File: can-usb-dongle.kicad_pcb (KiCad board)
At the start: 2 copper layers, 30 x 15 mm, 42 parts, among them SW1 SW_PUSH, U1 STM32F302C8T, U2 SN65HVD256, U3 NUF2042XV6, U4 MCP1700, U5 SiP32431, X1 16MHz 10ppm

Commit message: optimize traces
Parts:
- C12: moved to B.Cu
- moved C13 6.56 mm to (48.0, 38.5), turned to 180 degrees
- moved C11 4.26 mm to (54.5, 39.0), turned to 90 degrees
- moved R10 2.83 mm to (65.8, 40.8), turned to 270 degrees
- moved C6 2.75 mm to (57.8, 45.0)
- moved C5 2.70 mm to (59.0, 46.8)
- moved R2 2.66 mm to (49.0, 40.2)
- moved C9 2.55 mm to (59.5, 42.2), turned to 270 degrees
- moved C12 2.51 mm to (52.5, 39.5)
- moved C15 2.50 mm to (56.2, 43.0), turned to 90 degrees
- moved F1 2.26 mm to (51.0, 38.5), turned to 180 degrees
- moved R11 2.24 mm to (67.2, 40.8), turned to 270 degrees
- moved R5 1.82 mm to (49.2, 51.5), turned to 180 degrees
- moved R8 1.35 mm to (52.5, 48.8), turned to 90 degrees
- moved U4 1.25 mm to (52.8, 40.5)
- moved R4 1.12 mm to (64.5, 39.2), turned to 90 degrees
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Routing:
- net GND: track 52.0 -> 146.0 mm, vias 1 -> 7
- net VCC: track 38.8 -> 71.1 mm, vias 4 -> 5
- net /V_BUS_SENSE: track 19.6 -> 11.8 mm
- net /USB_D-: track 4.62 -> 11.9 mm
- net /USB_D+: track 10.3 -> 17.2 mm
- net /UART1_RX: track 11.8 -> 7.02 mm
- net /V_USB: track 26.7 -> 22.9 mm
- net /UART1_TX: track 10.8 -> 8.17 mm
- net /STATUS_LED: track 8.98 -> 6.57 mm
- net /NRST: track 9.60 -> 11.8 mm
- net Net-(C13-Pad1): track 10.4 -> 12.3 mm
- net Net-(CONN1-Pad4): track 10.3 -> 8.54 mm
- net /V_CAN_BUS: track 22.1 -> 23.7 mm
- net /CAN1_TX: track 5.64 -> 4.27 mm
- net Net-(D1-Pad2): track 0.00 -> 1.35 mm
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
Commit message: Better LED placement, change VCC routing
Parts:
- C10: moved to B.Cu
- moved R9 4.72 mm to (66.8, 47.0), turned to 90 degrees
- moved R3 3.26 mm to (63.5, 40.5)
- moved R4 3.26 mm to (61.2, 39.5)
- moved C10 2.26 mm to (67.8, 48.8), turned to 0 degrees
- moved R7 1.41 mm to (65.2, 50.2), turned to 0 degrees
- moved C14 1.00 mm to (68.2, 47.0)
- moved D2 0.35 mm to (67.8, 51.5)
- moved D3 0.35 mm to (67.8, 50.2)
- moved R6 0.35 mm to (65.2, 51.5), turned to 0 degrees
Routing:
- net GND: track 146.0 -> 170.7 mm
- net VCC: track 71.1 -> 64.9 mm
- net Net-(D3-Pad2): track 3.97 -> 0.00 mm
- net /V_BUS_SENSE: track 11.8 -> 8.48 mm
- net /V_CAN_BUS: track 23.7 -> 26.7 mm
- net /USB_D+: track 17.2 -> 19.1 mm
- net Net-(D2-Pad2): track 1.88 -> 0.00 mm
- net Net-(C7-Pad2): track 2.94 -> 4.76 mm
- net /CAN1_PWR_LED: track 7.46 -> 5.76 mm
- net /USB_D-: track 11.9 -> 13.2 mm
- net /CAN_SILENT: track 5.40 -> 4.67 mm

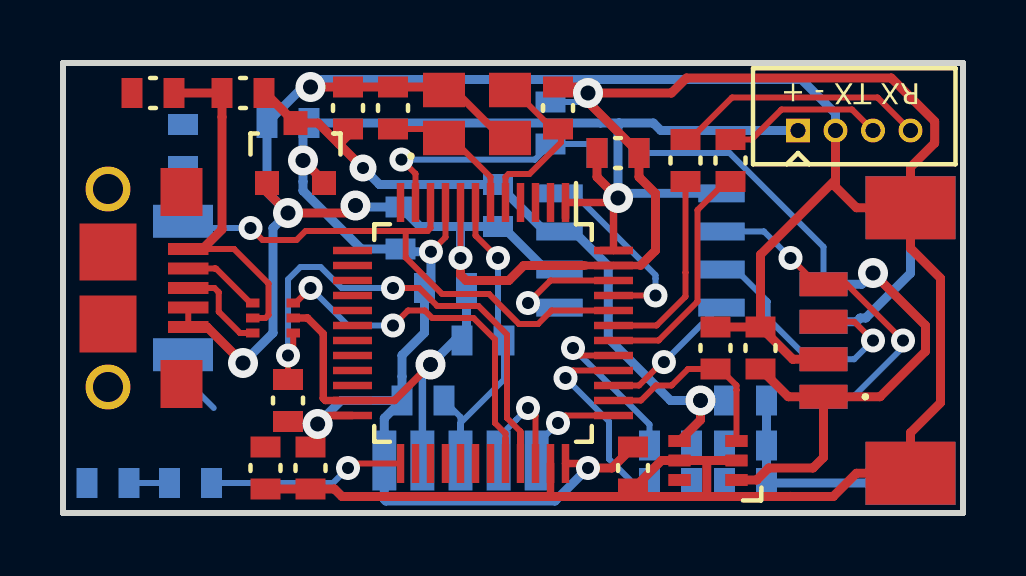
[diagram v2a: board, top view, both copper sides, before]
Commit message: Optimize VCC routing, redo power supply.
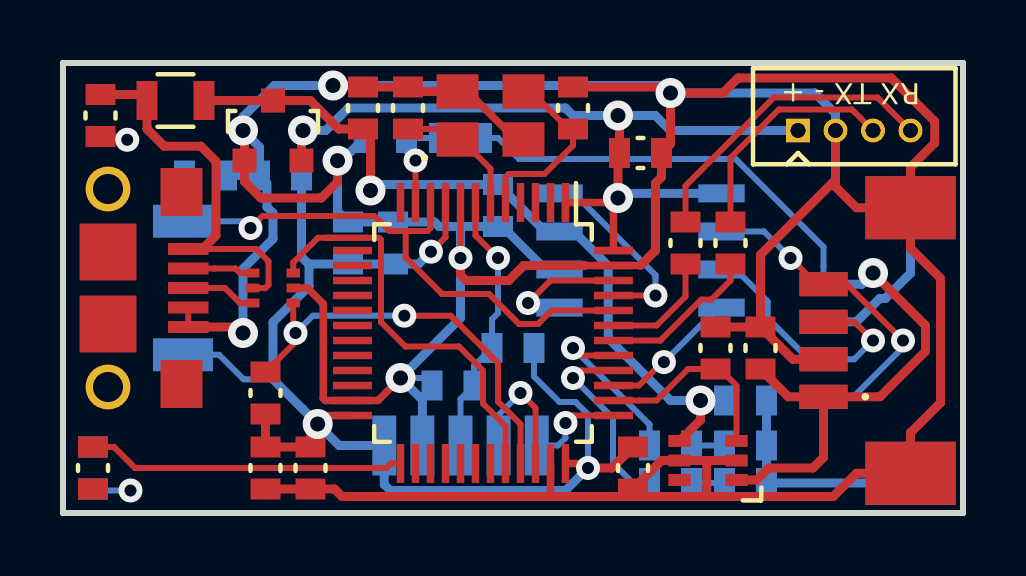
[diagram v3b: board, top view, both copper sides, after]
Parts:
- F1: footprint _std:_0603 -> Resistors_SMD:R_0805
- R5: moved to F.Cu
- moved R4 5.52 mm to (55.8, 40.0), turned to 180 degrees
- moved R3 5.27 mm to (58.2, 40.0)
- moved C6 3.58 mm to (54.5, 43.5), turned to 90 degrees
- moved R1 3.47 mm to (60.0, 47.0), turned to 180 degrees
- moved R5 3.29 mm to (46.0, 51.0), turned to 270 degrees
- moved R10 2.75 mm to (65.8, 43.5)
- moved R11 2.75 mm to (67.2, 43.5)
- moved F1 2.26 mm to (48.8, 38.8)
- moved C13 1.90 mm to (46.2, 39.2), turned to 270 degrees
- moved C5 1.80 mm to (58.0, 48.2)
- moved C12 1.77 mm to (52.2, 41.2)
- moved R2 1.25 mm to (49.8, 41.2), turned to 0 degrees
- moved U4 1.06 mm to (52.0, 39.8)
- moved U3 1.00 mm to (52.0, 45.0)
- moved R8 0.79 mm to (51.8, 48.5)
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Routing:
- net VCC: track 64.9 -> 73.3 mm, vias 5 -> 6
- net /V_CAN_BUS: track 26.7 -> 32.1 mm
- net /V_BUS_SENSE: track 8.48 -> 3.37 mm
- net /USB_D+: track 19.1 -> 14.0 mm
- net /STATUS_LED: track 6.57 -> 10.6 mm, vias 1 -> 0
- net GND: track 170.7 -> 174.5 mm, vias 7 -> 8
- net /NRST: track 11.8 -> 8.93 mm
- net /UART1_RX: track 6.64 -> 3.89 mm
- net /UART1_TX: track 7.88 -> 5.28 mm
- net /V_USB: track 23.4 -> 25.9 mm
- net Net-(CONN1-Pad3): track 5.45 -> 7.85 mm
- net /USB_D-: track 13.2 -> 15.2 mm, vias 2 -> 0
- net Net-(CONN1-Pad4): track 8.54 -> 10.4 mm
- net Net-(D3-Pad2): track 0.00 -> 1.10 mm
- net Net-(D2-Pad2): track 0.00 -> 1.10 mm
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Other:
- board text added: "+"

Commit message: Add GND fill zone, DRC check corrections
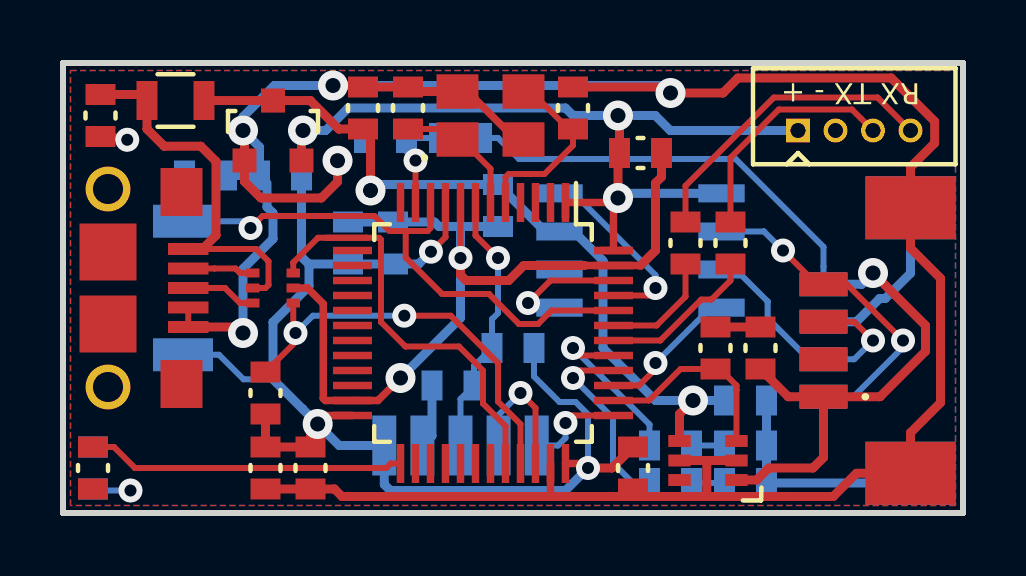
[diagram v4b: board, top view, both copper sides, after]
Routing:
- net GND: track 174.5 -> 142.4 mm
- added copper zone on B.Cu, net GND
- added copper zone on F.Cu, net GND

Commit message: Improve GND connection with vias
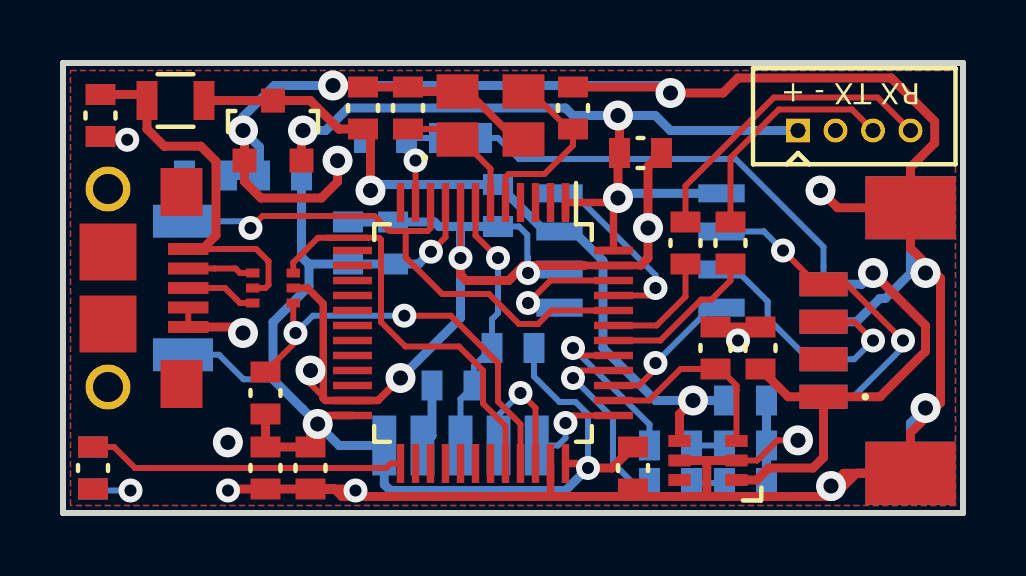
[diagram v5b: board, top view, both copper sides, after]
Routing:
- net GND: track 142.4 -> 155.2 mm, vias 8 -> 19
- net (no net): track 168.4 -> 168.5 mm, vias 0 -> 1
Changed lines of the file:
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@@
     (links 115)
     (no_connects 7)
-    (area 25.087299 28.495199 91.421702 60.2)
+    (area 44.899999 37.399999 75.100001 52.600001)
     (thickness 1.6)
     (drawings 9)
-    (tracks 445)
+    (tracks 479)
     (zones 0)
     (modules 42)
@@
   )
   (setup
-    (last_trace_width 0.3)
+    (last_trace_width 0.2)
     (user_trace_width 0.1524)
     (user_trace_width 0.1524)
@@
   (gr_line (start 45 52.5) (end 75 52.5) (layer Edge.Cuts) (width 0.2))
   (gr_line (start 45 37.5) (end 45 52.5) (layer Edge.Cuts) (width 0.2))
+  (segment (start 50.5 50.25) (end 50.5 50.149992) (width 0.3) (layer F.Cu) (net 0))
+  (segment (start 50.5 50.149992) (end 50.495998 50.14599) (width 0.3) (layer F.Cu) (net 0))
+  (via (at 50.495998 50.14599) (size 1) (drill 0.5) (layers F.Cu B.Cu) (net 0))
   (segment (start 28.3079 28.8202) (end 28.1174 29.0107) (width 0.25) (layer Dwgs.User) (net 0))
   (segment (start 25.4123 31.7158) (end 28.3079 28.8202) (width 0.25) (layer Dwgs.User) (net 0))
@@
   (segment (start 61.769981 50.869981) (end 61.75 50.85) (width 0.25) (layer F.Cu) (net 1))
   (via (at 62.5 51) (size 0.8) (drill 0.4) (layers F.Cu B.Cu) (net 1))
+  (segment (start 68.25 46.3) (end 67.95 46.3) (width 0.2) (layer F.Cu) (net 2))
+  (segment (start 67.95 46.3) (end 67.5 46.75) (width 0.2) (layer F.Cu) (net 2))
+  (via (at 67.5 46.75) (size 0.8) (drill 0.4) (layers F.Cu B.Cu) (net 2))
+  (segment (start 67.44996 50.75) (end 68.13844 50.75) (width 0.2) (layer F.Cu) (net 2))
+  (segment (start 68.13844 50.75) (end 68.810798 50.077642) (width 0.2) (layer F.Cu) (net 2))
+  (via (at 69.49999 50.077642) (size 1) (drill 0.5) (layers F.Cu B.Cu) (net 2))
+  (segment (start 68.810798 50.077642) (end 69.49999 50.077642) (width 0.2) (layer F.Cu) (net 2))
+  (segment (start 54.65 48.75) (end 53.8 48.75) (width 0.2) (layer F.Cu) (net 2))
+  (segment (start 53.8 48.75) (end 53.25 48.2) (width 0.2) (layer F.Cu) (net 2))
+  (segment (start 53.25 48.2) (end 53.25 47.75) (width 0.2) (layer F.Cu) (net 2))
+  (via (at 53.25 47.75) (size 1) (drill 0.5) (layers F.Cu B.Cu) (net 2))
+  (segment (start 64.25 44.25) (end 64.5 44) (width 0.3) (layer F.Cu) (net 2))
+  (segment (start 64.5 44) (end 64.5 43) (width 0.3) (layer F.Cu) (net 2))
+  (segment (start 64.95 40.5) (end 64.5 40.95) (width 0.3) (layer F.Cu) (net 2))
+  (segment (start 64.5 40.95) (end 64.5 43) (width 0.3) (layer F.Cu) (net 2))
+  (via (at 64.5 43) (size 1) (drill 0.5) (layers F.Cu B.Cu) (net 2))
+  (segment (start 73.25 42.325) (end 70.825 42.325) (width 0.3) (layer F.Cu) (net 2))
+  (segment (start 70.825 42.325) (end 70.25 41.75) (width 0.3) (layer F.Cu) (net 2))
+  (via (at 70.25 41.75) (size 1) (drill 0.5) (layers F.Cu B.Cu) (net 2))
+  (segment (start 73.25 42.325) (end 73.25 44) (width 0.3) (layer B.Cu) (net 2))
+  (segment (start 73.25 44) (end 73.75 44.5) (width 0.3) (layer B.Cu) (net 2))
+  (via (at 73.75 44.5) (size 1) (drill 0.5) (layers F.Cu B.Cu) (net 2))
+  (segment (start 73.25 51.175) (end 71.027096 51.175) (width 0.3) (layer F.Cu) (net 2))
+  (segment (start 71.027096 51.175) (end 70.601048 51.601048) (width 0.3) (layer F.Cu) (net 2))
+  (via (at 70.601048 51.601048) (size 1) (drill 0.5) (layers F.Cu B.Cu) (net 2))
+  (segment (start 73.25 51.175) (end 73.25 49.5) (width 0.3) (layer B.Cu) (net 2))
+  (segment (start 73.25 49.5) (end 73.75 49) (width 0.3) (layer B.Cu) (net 2))
+  (via (at 73.75 49) (size 1) (drill 0.5) (layers F.Cu B.Cu) (net 2))
+  (segment (start 53.25 51.7) (end 54.7 51.7) (width 0.3) (layer F.Cu) (net 2))
+  (segment (start 54.7 51.7) (end 54.75 51.75) (width 0.3) (layer F.Cu) (net 2))
+  (via (at 54.75 51.75) (size 0.8) (drill 0.4) (layers F.Cu B.Cu) (net 2))
+  (segment (start 51.75 51.7) (end 50.55 51.7) (width 0.3) (layer F.Cu) (net 2))
+  (via (at 50.5 51.75) (size 0.8) (drill 0.4) (layers F.Cu B.Cu) (net 2))
+  (segment (start 50.55 51.7) (end 50.5 51.75) (width 0.3) (layer F.Cu) (net 2))
+  (segment (start 60.474999 43.224999) (end 60.474999 44.284999) (width 0.2) (layer B.Cu) (net 2))
+  (segment (start 60.474999 44.284999) (end 60.575 44.385) (width 0.2) (layer B.Cu) (net 2))
+  (segment (start 60.575 44.385) (end 61.55 44.385) (width 0.2) (layer B.Cu) (net 2))
+  (segment (start 59.5 42.95) (end 60.2 42.95) (width 0.2) (layer B.Cu) (net 2))
+  (segment (start 60.2 42.95) (end 60.474999 43.224999) (width 0.2) (layer B.Cu) (net 2))
+  (segment (start 61.55 44.385) (end 61.075 44.385) (width 0.2) (layer B.Cu) (net 2))
+  (segment (start 60.5 43.963998) (end 60.5 44.5) (width 0.2) (layer B.Cu) (net 2))
+  (via (at 60.5 44.5) (size 0.8) (drill 0.4) (layers F.Cu B.Cu) (net 2))
   (segment (start 66.75 46.3) (end 68.25 46.3) (width 0.3) (layer F.Cu) (net 2))
   (segment (start 57.3 48.25) (end 57.3 49.93) (width 0.3) (layer B.Cu) (net 2))
@@
   (segment (start 51.05 39.8) (end 51 39.75) (width 0.3) (layer F.Cu) (net 2))
   (via (at 51 39.75) (size 1) (drill 0.5) (layers F.Cu B.Cu) (net 2))
-  (segment (start 64.75 43.75) (end 64.75 41.5) (width 0.3) (layer F.Cu) (net 2))
-  (segment (start 64.75 41.5) (end 64.95 41.3) (width 0.3) (layer F.Cu) (net 2))
-  (segment (start 64.95 41.3) (end 64.95 40.5) (width 0.3) (layer F.Cu) (net 2))
   (segment (start 70.35 46.125) (end 71.45 46.125) (width 0.3) (layer B.Cu) (net 2))
   (segment (start 71.45 46.125) (end 72.224999 45.350001) (width 0.3) (layer B.Cu) (net 2))
@@
   (segment (start 73.25 44.508002) (end 73.25 43.675) (width 0.3) (layer B.Cu) (net 2))
   (segment (start 73.25 43.675) (end 73.25 42.325) (width 0.3) (layer B.Cu) (net 2))
-  (segment (start 52.000001 43.360001) (end 52.000001 42.500001) (width 0.3) (layer B.Cu) (net 2))
-  (segment (start 52.000001 42.500001) (end 51.8 42.3) (width 0.3) (layer B.Cu) (net 2))
-  (segment (start 51.8 42.3) (end 51.8 41.5) (width 0.3) (layer B.Cu) (net 2))
   (segment (start 58.338515 42.95) (end 57.532674 42.95) (width 0.3) (layer B.Cu) (net 2))
   (segment (start 56 42.8) (end 57.382674 42.8) (width 0.3) (layer B.Cu) (net 2))
   (segment (start 57.382674 42.8) (end 57.532674 42.95) (width 0.3) (layer B.Cu) (net 2))
   (segment (start 54.5 42.8) (end 56 42.8) (width 0.3) (layer B.Cu) (net 2))
-  (segment (start 51 46.5) (end 51 44.360002) (width 0.3) (layer B.Cu) (net 2))
-  (segment (start 51 44.360002) (end 52.000001 43.360001) (width 0.3) (layer B.Cu) (net 2))
   (segment (start 54 38.25) (end 54.95 38.25) (width 0.3) (layer F.Cu) (net 2))
   (segment (start 54.95 38.25) (end 55 38.3) (width 0.3) (layer F.Cu) (net 2))
@@
   (segment (start 74.250011 48.824989) (end 73.25 49.825) (width 0.3) (layer F.Cu) (net 2))
   (segment (start 73.25 49.825) (end 73.25 51.175) (width 0.3) (layer F.Cu) (net 2))
-  (segment (start 64.75 43.75) (end 64.25 44.25) (width 0.3) (layer F.Cu) (net 2))
-  (segment (start 68.45 51.5) (end 72.925 51.5) (width 0.3) (layer B.Cu) (net 2))
-  (segment (start 72.925 51.5) (end 73.25 51.175) (width 0.3) (layer B.Cu) (net 2))
   (segment (start 68.45 50.25) (end 68.45 51.5) (width 0.3) (layer B.Cu) (net 2))
   (segment (start 68.45 48.75) (end 68.45 50.25) (width 0.3) (layer B.Cu) (net 2))

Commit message: Add CVRA logo, silk screen text
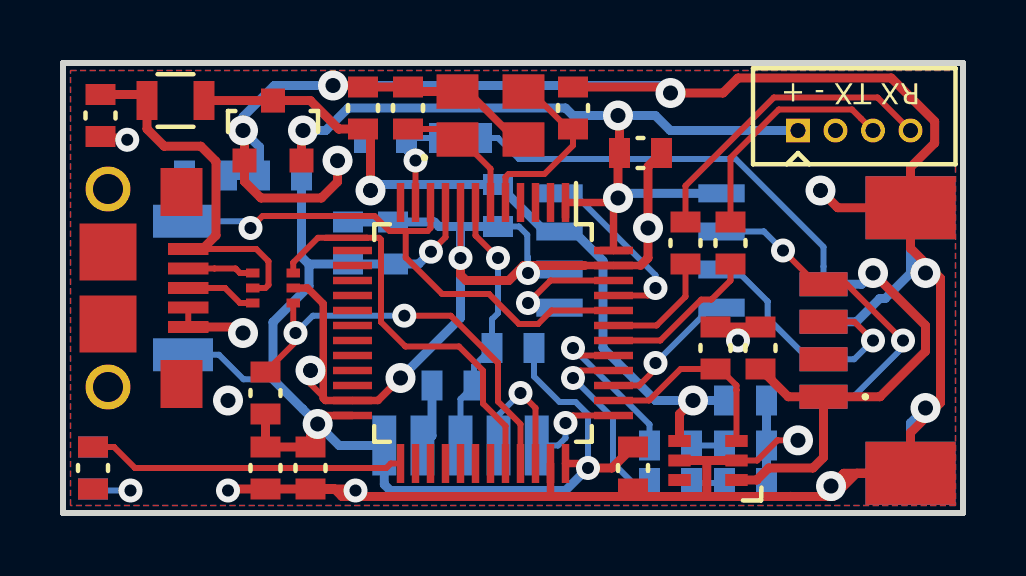
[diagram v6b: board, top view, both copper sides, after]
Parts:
- added G***: LOGO, _logo:CVRA-logo-small, B.Cu at (48.8, 50.2)
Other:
- board text added: "CAN"
- board text added: "CAN to USB dongle - Rev A"
- board text added: "CVRA"
- board text added: "PWR"
